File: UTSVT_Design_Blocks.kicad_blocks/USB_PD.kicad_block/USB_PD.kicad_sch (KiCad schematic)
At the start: 0 parts

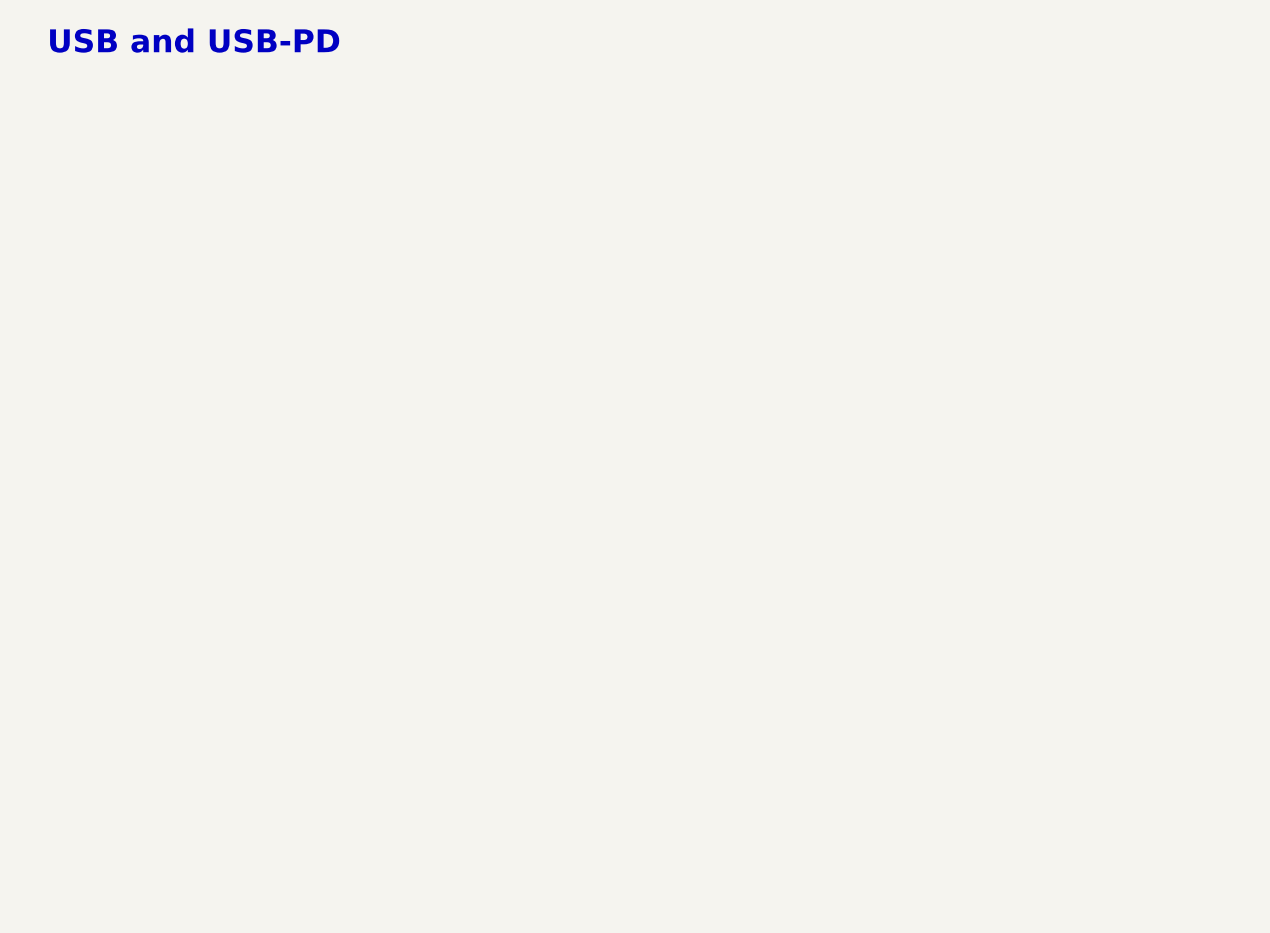
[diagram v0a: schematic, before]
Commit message: added USB port, temporary PD controller and boost converter
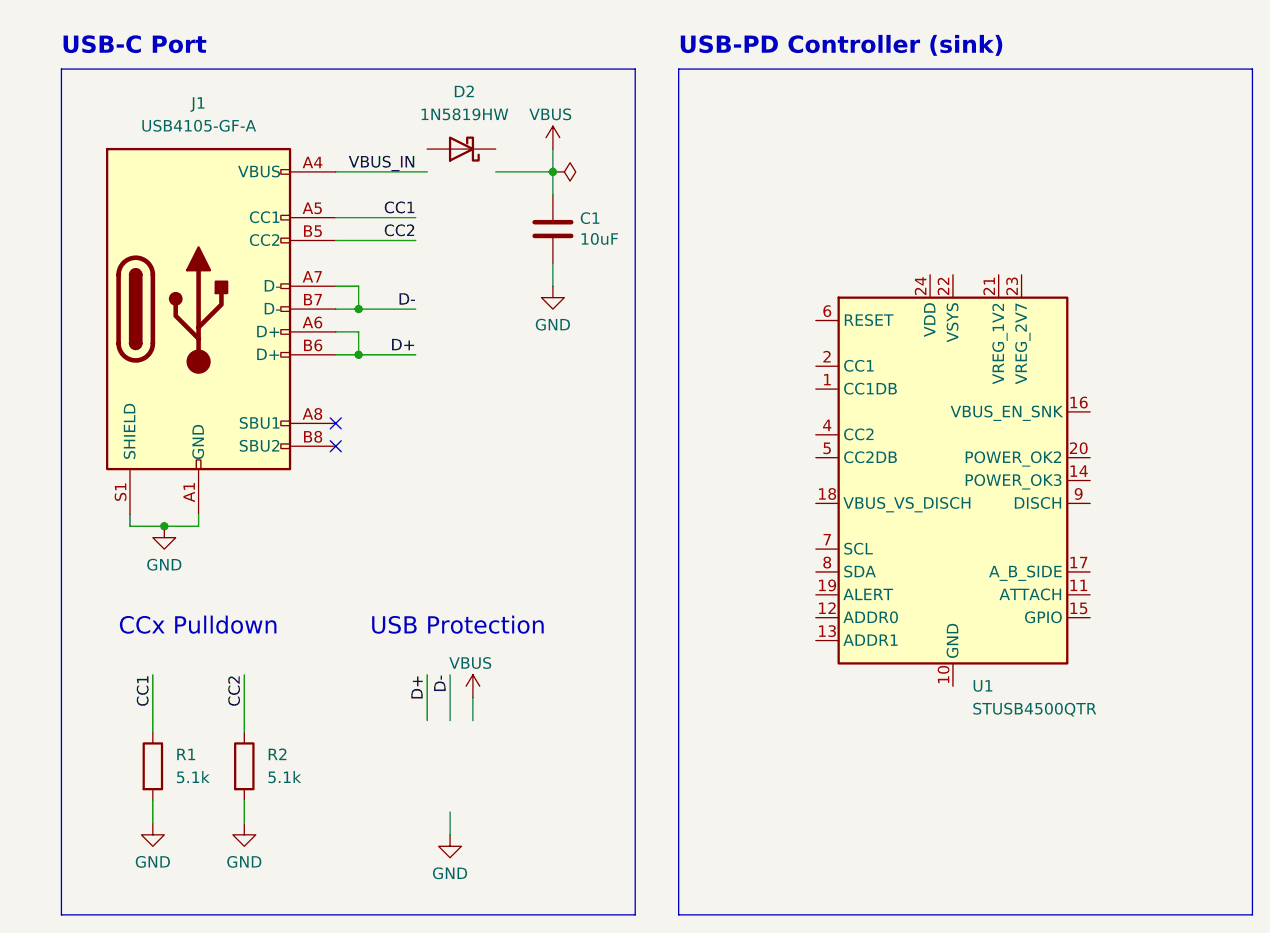
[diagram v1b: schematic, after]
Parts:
- added C1: 10uF, Capacitor_SMD:C_0805_2012Metric_Pad1.18x1.45mm_HandSolder, symbol Device:C
- added D2: 1N5819HW, Diode_SMD:D_SOD-123, symbol Device:D_Schottky
- added J1: USB4105-GF-A, UTSVT_Connectors:USB_C_Receptacle_GCT_USB4105-xx-A_16P_TopMnt_Horizontal, symbol Connector:USB_C_Receptacle_USB2.0_16P
- added R1, R2: 5.1k, Resistor_SMD:R_0603_1608Metric_Pad0.98x0.95mm_HandSolder, symbol Device:R
- added U1: STUSB4500QTR, Package_DFN_QFN:QFN-24-1EP_4x4mm_P0.5mm_EP2.7x2.7mm, symbol Interface_USB:STUSB4500QTR
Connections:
- new net: U1.10 (GND), U1.25 (GND)
- new net CC1: J1.A5 (CC1), R1.1
- new net CC2: J1.B5 (CC2), R2.1
- new net D+: J1.A6 (D+), J1.B6 (D+)
- new net D-: J1.A7 (D-), J1.B7 (D-)
- new net GND: C1.2, J1.A1 (GND), J1.A12 (GND), J1.B1 (GND), J1.B12 (GND), J1.S1 (SHIELD), R1.2, R2.2
- new net VBUS: C1.1
- new net VBUS_IN: J1.A4 (VBUS), J1.A9 (VBUS), J1.B4 (VBUS), J1.B9 (VBUS)
- no-connect marks 0 -> 2
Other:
- note added: "CCx Pulldown"
- note added: "USB Protection"
- note added: "USB-C Port"
- note added: "USB-PD Controller (sink)"
- note removed: "USB and USB-PD"

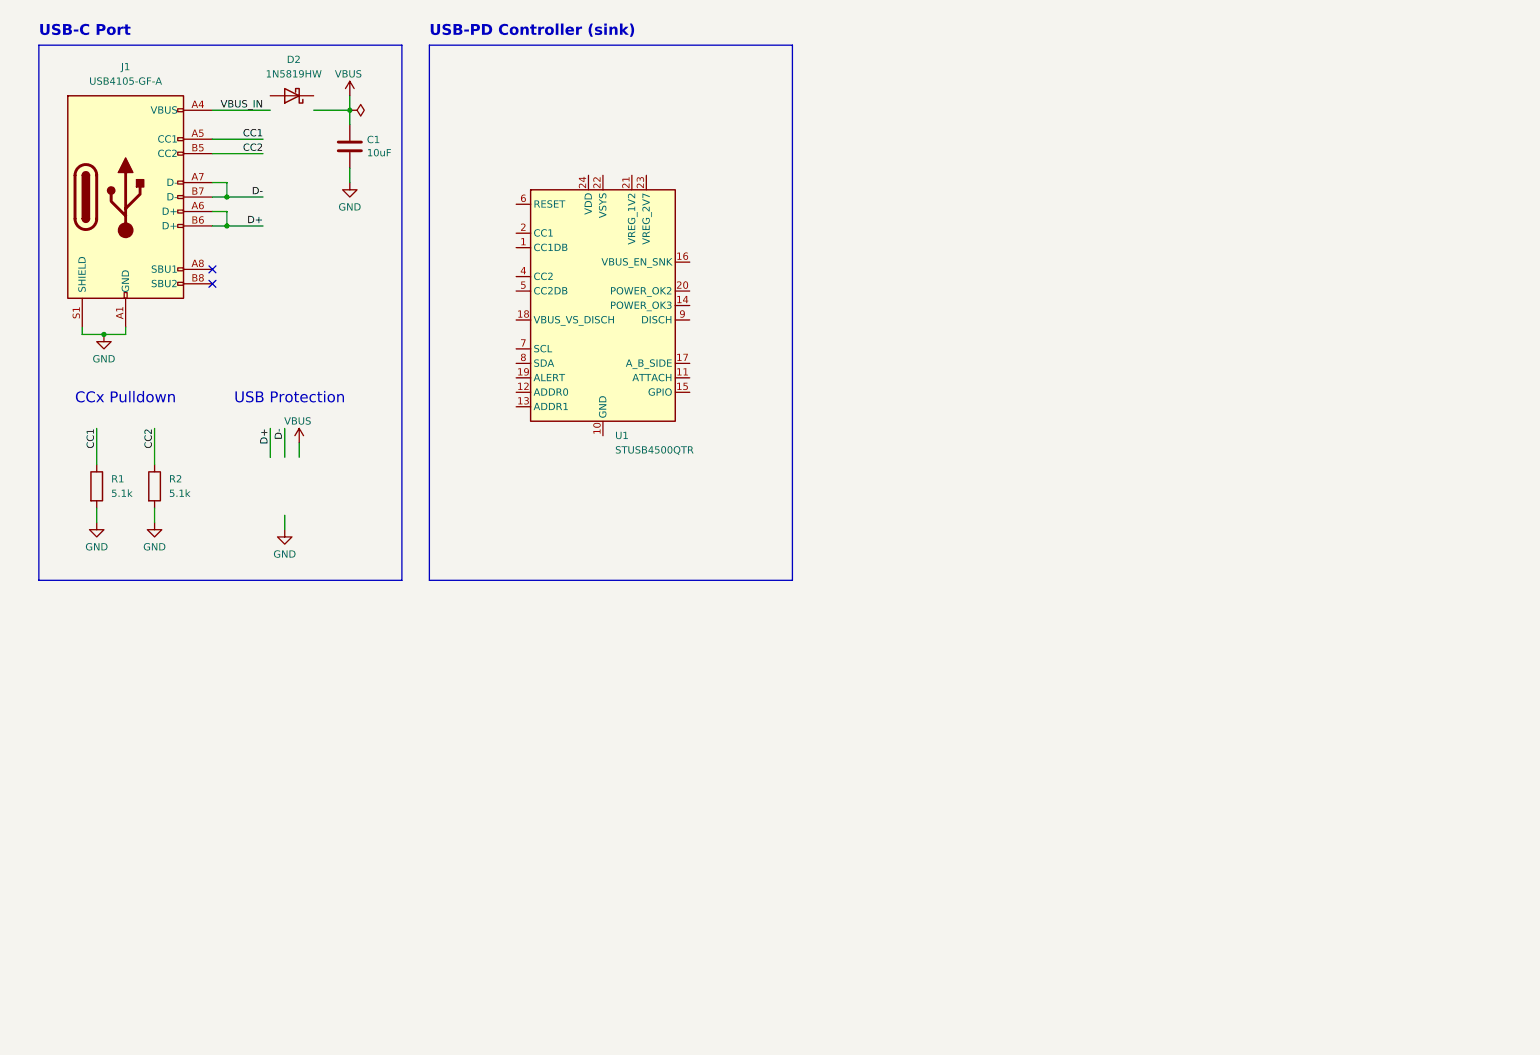
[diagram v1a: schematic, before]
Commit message: added CYPD3177
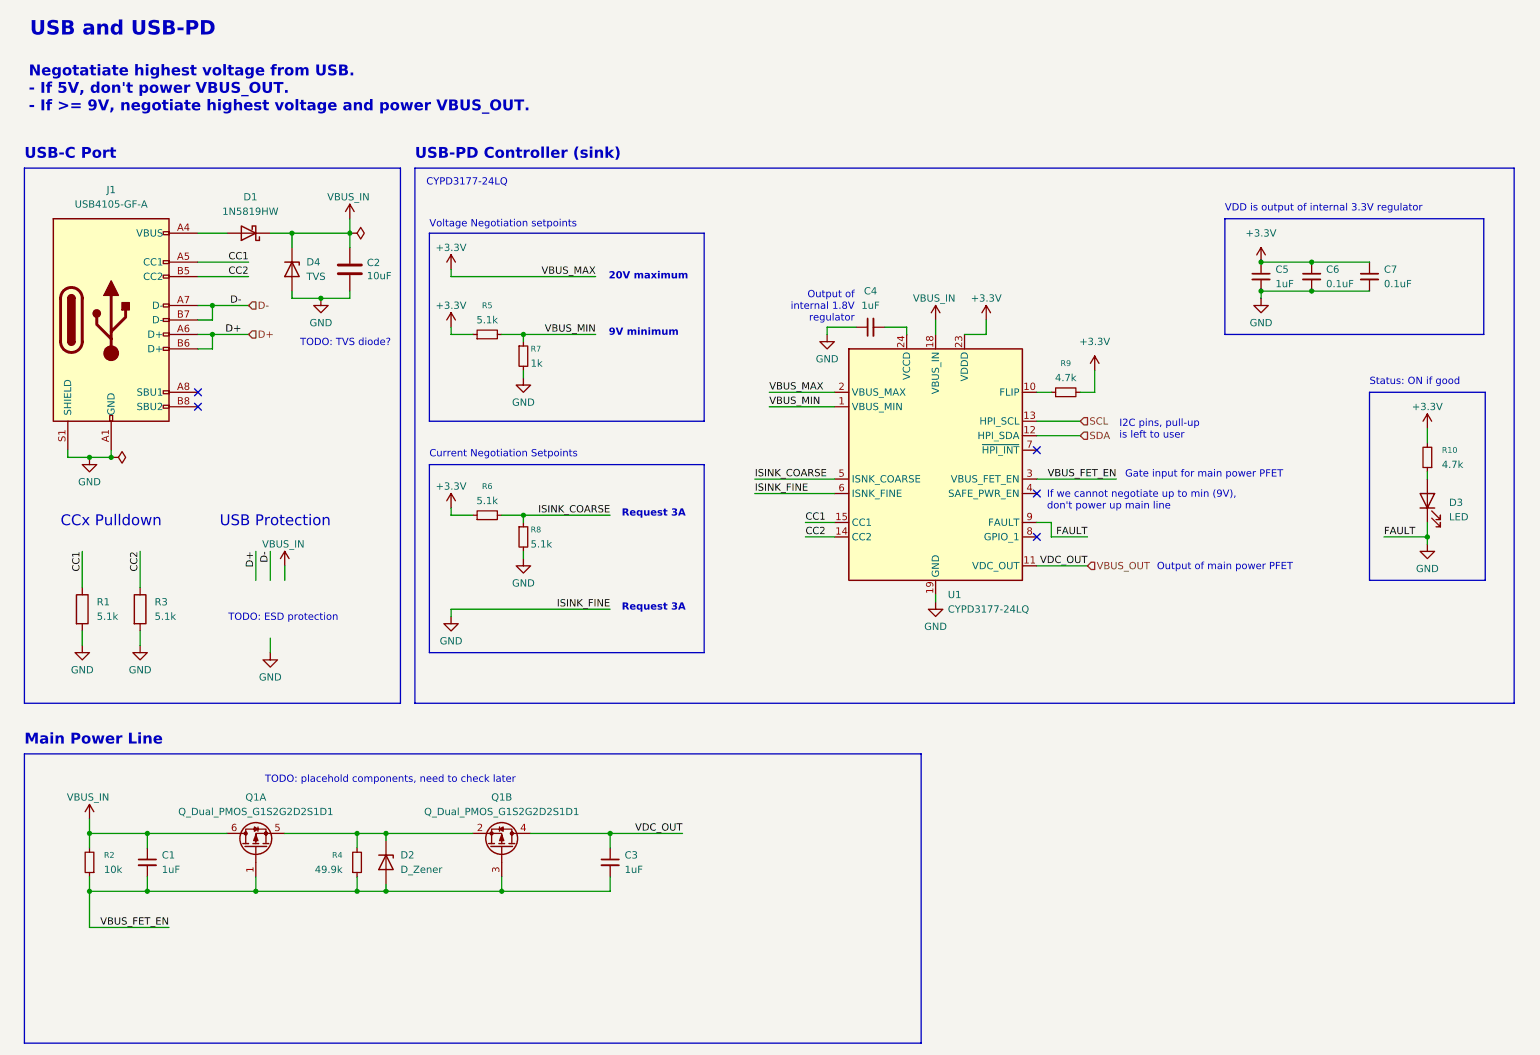
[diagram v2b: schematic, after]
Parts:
- removed C1: 10uF, Capacitor_SMD:C_0805_2012Metric_Pad1.18x1.45mm_HandSolder, symbol Device:C
- removed D2: 1N5819HW, Diode_SMD:D_SOD-123, symbol Device:D_Schottky
- removed R2: 5.1k, Resistor_SMD:R_0603_1608Metric_Pad0.98x0.95mm_HandSolder, symbol Device:R
- removed U1: STUSB4500QTR, Package_DFN_QFN:QFN-24-1EP_4x4mm_P0.5mm_EP2.7x2.7mm, symbol Interface_USB:STUSB4500QTR
- added C1, C3, C4, C5: 1uF, symbol Device:C_Small
- added C2: 10uF, Capacitor_SMD:C_0805_2012Metric_Pad1.18x1.45mm_HandSolder, symbol Device:C
- added C6, C7: 0.1uF, symbol Device:C_Small
- added D1: 1N5819HW, Diode_SMD:D_SOD-123, symbol Device:D_Schottky
- added D2: D_Zener, symbol Device:D_Zener
- added D3: LED, symbol Device:LED
- added D4: TVS, symbol Device:D_Zener
- added Q1: Q_Dual_PMOS_G1S2G2D2S1D1, symbol Transistor_FET:Q_Dual_PMOS_G1S2G2D2S1D1
- added R10, R9: 4.7k, symbol Device:R_Small
- added R2: 10k, symbol Device:R_Small
- added R3: 5.1k, Resistor_SMD:R_0603_1608Metric_Pad0.98x0.95mm_HandSolder, symbol Device:R
- added R4: 49.9k, symbol Device:R_Small
- added R5, R6, R8: 5.1k, symbol Device:R_Small
- added R7: 1k, symbol Device:R_Small
- added U1: CYPD3177-24LQ, Package_DFN_QFN:QFN-24-1EP_4x4mm_P0.5mm_EP2.75x2.75mm, symbol Interface_USB:CYPD3177-24LQ
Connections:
- net CC1: now also U1.15 (CC1)
- net CC2: now also R3.1, U1.14 (CC2)
- net GND: now also C2.2, C4.1, C5.2, C6.2, C7.2, D3.1 (K), D4.2 (A), R3.2, R7.2, R8.2, U1.19 (GND), U1.22 (GND), U1.25 (GND), U1.6 (ISNK_FINE), U1.9 (FAULT)
- net VBUS_IN: now also C1.1, C2.1, D1.1 (K), D4.1 (K), Q1.6 (D), R2.2, U1.18 (VBUS_IN); no longer J1.A4 (VBUS), J1.A9 (VBUS), J1.B4 (VBUS), J1.B9 (VBUS)
- new net: D3.2 (A), R10.1
- new net: R9.1, U1.10 (FLIP)
- new net: C4.2, U1.24 (VCCD)
- new net: D1.2 (A), J1.A4 (VBUS), J1.A9 (VBUS), J1.B4 (VBUS), J1.B9 (VBUS)
- new net: D2.1 (K), Q1.2 (S), Q1.5 (S), R4.2
- new net +3.3V: C5.1, C6.1, C7.1, R10.2, R5.1, R6.1, R9.2, U1.2 (VBUS_MAX), U1.23 (VDDD)
- new net ISINK_COARSE: R6.2, R8.1, U1.5 (ISNK_COARSE)
- new net SCL: U1.13 (HPI_SCL)
- new net SDA: U1.12 (HPI_SDA)
- new net VBUS_FET_EN: C1.2, C3.2, D2.2 (A), Q1.1 (G), Q1.3 (G), R2.1, R4.1, U1.3 (VBUS_FET_EN)
- new net VBUS_MIN: R5.2, R7.1, U1.1 (VBUS_MIN)
- new net VBUS_OUT: C3.1, Q1.4 (D), U1.11 (VDC_OUT)
- no-connect marks 2 -> 5
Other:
- note added: "20V maximum"
- note added: "9V minimum"
- note added: "CYPD3177-24LQ"
- note added: "Current Negotiation Setpoints"
- note added: "Gate input for main power PFET"
- note added: "I2C pins, pull-up is left to user"
- note added: "If we cannot negotiate up to min (9V), don't power up main line"
- note added: "Main Power Line"
- note added: "Negotatiate highest voltage from USB. - If 5V, don't power VBUS_OUT. - If >= 9V, negotiate highest voltage and power VBUS_OUT."
- note added: "Output of internal 1.8V regulator"
- note added: "Output of main power PFET"
- note added: "Request 3A"
- note added: "Status: ON if good"
- note added: "TODO: ESD protection"
- note added: "TODO: TVS diode?"
- note added: "TODO: placehold components, need to check later"
- note added: "USB and USB-PD"
- note added: "VDD is output of internal 3.3V regulator"
- note added: "Voltage Negotiation setpoints"

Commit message: power paths
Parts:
- added Q2: Q_Dual_PMOS_G1S2G2D2S1D1, symbol Transistor_FET:Q_Dual_PMOS_G1S2G2D2S1D1
- added R11, R13: 1k, symbol Device:R_Small
- added R12: 49.9k, symbol Device:R_Small
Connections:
- net VBUS_FET_EN: now also R13.2; no longer C1.2, C3.2, D2.2 (A), Q1.1 (G), Q1.3 (G), R2.1, R4.1
- net VBUS_IN: now also Q2.6 (D), R12.2
- net SAFE_PWR_EN: now reaches U1.4 (SAFE_PWR_EN)
- net SAFE_PWR_EN: now also R11.2
- new net: C1.2, C3.2, D2.2 (A), Q1.1 (G), Q1.3 (G), R13.1, R2.1, R4.1
- new net: Q2.1 (G), Q2.3 (G), R11.1, R12.1
- new net: Q2.2 (S), Q2.5 (S)
- new net 5V_OUT: Q2.4 (D)
- no-connect marks 5 -> 4
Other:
- note added: "- If >= 9V, negotiate highest voltage and power VBUS_OUT. - If 5V, power 5V_OUT."
- note added: "5V Power (if we fail to negotiate)"
- note added: "Gate input for 5V power PFET"
- note added: "If we cannot negotiate up to min (9V), safe power line is driven instead."
- note added: "Internal 1.8V regulator"
- note added: "Power Path"
- note added: "USB PD Path"
- note removed: "If we cannot negotiate up to min (9V), don't power up main line"
- note removed: "Main Power Line"
- note removed: "Negotatiate highest voltage from USB. - If 5V, don't power VBUS_OUT. - If >= 9V, negotiate highest voltage and power VBUS_OUT."
- note removed: "Output of internal 1.8V regulator"
- moved on the sheet: C1, C3, D2, Q1A, Q1B, R1, R2, R3, R4
